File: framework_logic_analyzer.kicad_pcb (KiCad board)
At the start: 4 copper layers, 54 x 43 mm, 116 parts, among them IC1 TXU0104QWBQARQ1, IC2 TXU0104QWBQARQ1, IC3 TXU0104QWBQARQ1, IC4 TXU0104QWBQARQ1, IC5 CYUSB3014-BZXC, IC6 XC9285B18CMR-G, J1 10152803-00011LF, J3 Conn_ARM_JTAG_SWD_10, J4 6101XX249121_610108249121, J5 6101XX249121_610108249121, J6 6101XX249121_610108249121, J7 6101XX249121_610108249121, Q1 MMBT3904, Q2 MMBT3904, Q3 MMBT3904, U1 NCP360SNT1G, U2 TUSB321RWBR, U4 SC189CSKTRT, U5 M24M02-DR, U7 TUSB542RWQR, Y1 19.200 MHz

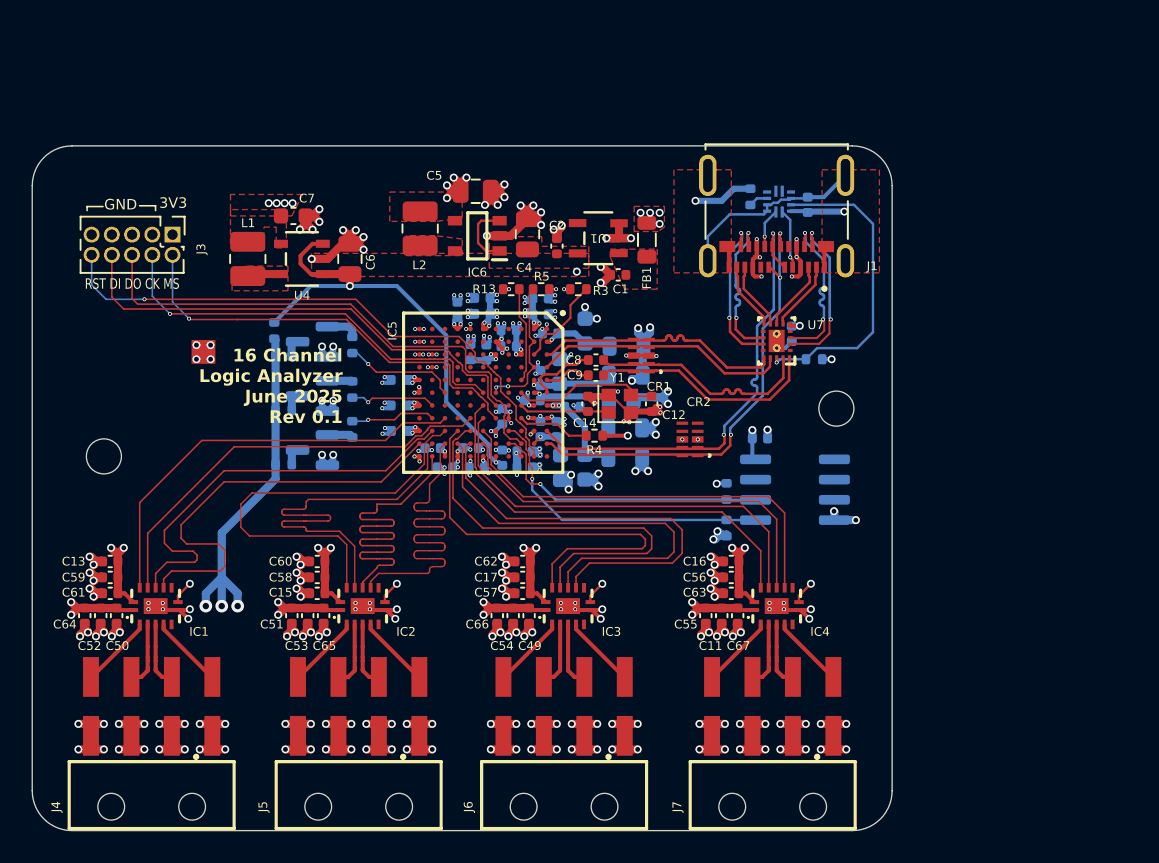
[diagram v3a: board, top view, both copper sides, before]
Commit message: add AC caps for redriver; fix ERC and DRC errors
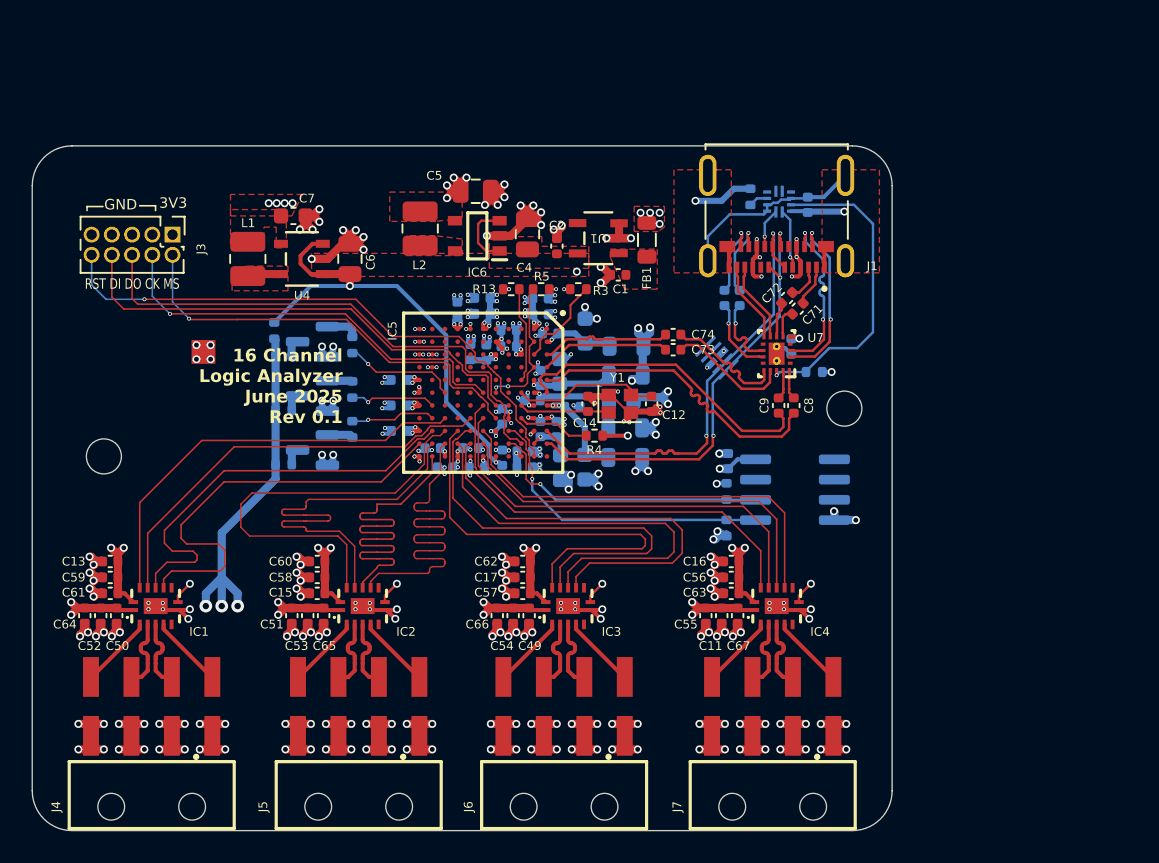
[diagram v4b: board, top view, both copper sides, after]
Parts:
- removed CR1: SP3010-04UTG, SP3010:UDFEN-10_MO229_LTF
- added C69: 100n 25V, Capacitor_SMD:C_0402_1005Metric, B.Cu at (152.9, 72.7)
- added C70: 100n 25V, Capacitor_SMD:C_0402_1005Metric, B.Cu at (153.8, 72.7)
- added C71: 100n 25V, Capacitor_SMD:C_0402_1005Metric, F.Cu at (157.5, 73.3)
- added C72: 100n 25V, Capacitor_SMD:C_0402_1005Metric, F.Cu at (156.8, 72.7)
- added C73: 100n 25V, Capacitor_SMD:C_0402_1005Metric, F.Cu at (149.7, 75.9)
- added C74: 100n 25V, Capacitor_SMD:C_0402_1005Metric, F.Cu at (149.7, 75.0)
- CR2: moved to B.Cu
- moved C8 12.7 mm to (157.2, 79.4), turned to 90 degrees
- moved C9 11.6 mm to (156.3, 79.4), turned to 90 degrees
- moved CR2 5.39 mm to (152.4, 76.4), turned to 45 degrees
- moved C48 2.46 mm to (153.1, 82.9), turned to 90 degrees
- moved C3 0.80 mm to (157.1, 75.7)
- moved U7 0.80 mm to (156.2, 76.2)
- moved R2 0.80 mm to (158.5, 77.3)
- moved H2 0.50 mm to (160.4, 79.6)
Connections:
- C8 pad 1: /USB-C/SS_TX- -> /USB-C/SS_TX+
- C8 pad 2: /SS_AC_TX- -> /USB-C/SS_REDRIVE_TX+
- C9 pad 1: /USB-C/SS_TX+ -> /USB-C/SS_TX-
- C9 pad 2: /SS_AC_TX+ -> /USB-C/SS_REDRIVE_TX-
- IC5 pad A5: /SS_AC_TX+ -> /USB-C/SS_TX+
- IC5 pad A6: /SS_AC_TX- -> /USB-C/SS_TX-
- U7 pad 11: /USB-C/SS_TX2- -> /USB-C/SS_REDRIVE_TX2-
- U7 pad 12: /USB-C/SS_TX2+ -> /USB-C/SS_REDRIVE_TX2+
- U7 pad 14: /USB-C/SS_RX- -> /USB-C/SS_REDRIVE_RX-
- U7 pad 15: /USB-C/SS_RX+ -> /USB-C/SS_REDRIVE_RX+
- U7 pad 17: /USB-C/SS_TX- -> /USB-C/SS_REDRIVE_TX-
- U7 pad 18: /USB-C/SS_TX+ -> /USB-C/SS_REDRIVE_TX+
- U7 pad 6: /USB-C/SS_TX1+ -> /USB-C/SS_REDRIVE_TX1+
- U7 pad 7: /USB-C/SS_TX1- -> /USB-C/SS_REDRIVE_TX1-
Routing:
- net /USB-C/SS_RX+: track 16.0 -> 8.15 mm
- net /USB-C/SS_RX-: track 16.0 -> 8.14 mm
- net /USB-C/SS_REDRIVE_RX+: track 0.00 -> 7.79 mm
- net /USB-C/SS_REDRIVE_RX-: track 0.00 -> 7.75 mm
- net /USB-C/SS_TX-: track 14.4 -> 19.5 mm
- net /USB-C/SS_TX+: track 14.5 -> 19.4 mm
- net /USB-C/SS_TX2+: track 9.88 -> 4.97 mm, vias 2 -> 1
- net /USB-C/SS_REDRIVE_TX2+: track 0.00 -> 4.87 mm, vias 0 -> 1
- net /USB-C/SS_TX2-: track 9.83 -> 4.97 mm, vias 2 -> 1
- net /USB-C/SS_REDRIVE_TX2-: track 0.00 -> 4.84 mm, vias 0 -> 1
- net /SS_AC_TX-: track 4.60 -> 0.00 mm
- net /SS_AC_TX+: track 2.99 -> 0.00 mm
- net /USB-C/SS_REDRIVE_TX1-: track 0.00 -> 2.24 mm
- net /USB-C/SS_TX1-: track 4.46 -> 2.31 mm
- net GND: track 199.1 -> 197.1 mm, vias 267 -> 265
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
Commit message: initial TurboCase implementation
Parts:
- added ?: , Cutout_Pinheader_02x08_254, F.Cu at (129.9, 106.6)
- added ?: , Cutout_Pinheader_02x08_254, F.Cu at (116.9, 106.6)
- added ?: , Cutout_Pinheader_02x08_254, F.Cu at (142.9, 106.6)
- added ?: , Cutout_TypeC, F.Cu at (156.2, 62.6)
- added ?: , Cutout_Pinheader_02x08_254, F.Cu at (155.9, 106.6)

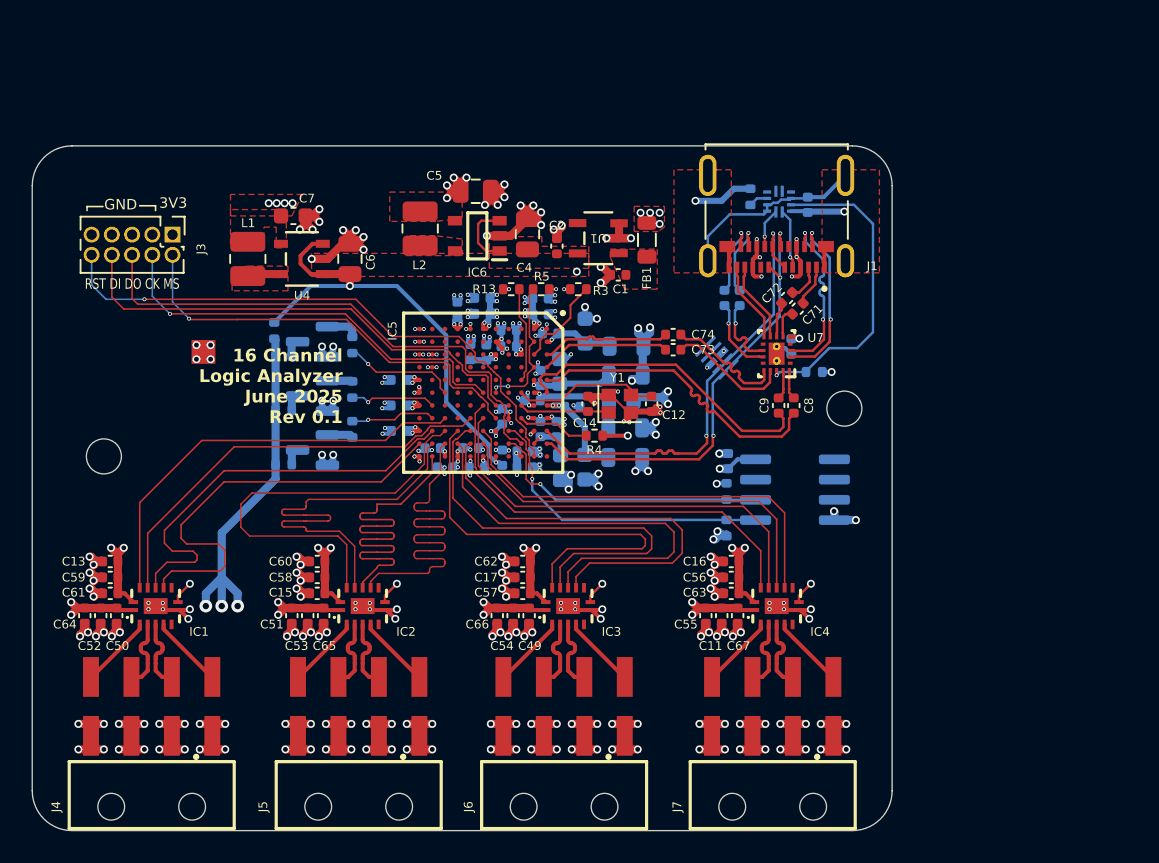
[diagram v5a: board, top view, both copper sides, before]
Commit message: start reworking the usb3c to add ESD and better impedance matching
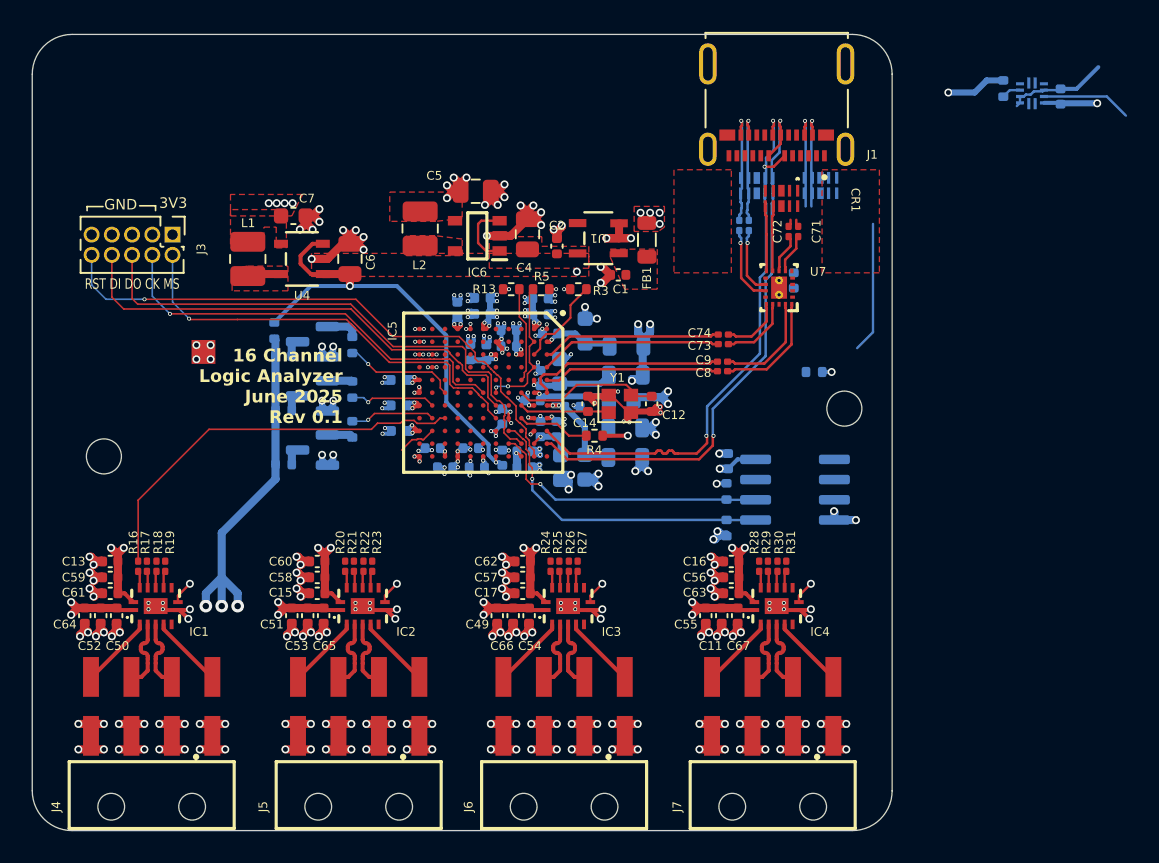
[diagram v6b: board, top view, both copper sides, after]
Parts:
- added CR1: SP3010-04UTG, SP3010:UDFEN-10_MO229_LTF, F.Cu at (156.4, 66.4)
- added CR3: SP3010-04UTG, SP3010:UDFEN-10_MO229_LTF, B.Cu at (158.9, 65.6)
- added R16: 50R 1%, Resistor_SMD:R_0201_0603Metric, F.Cu at (116.0, 89.5)
- added R17: 50R 1%, Resistor_SMD:R_0201_0603Metric, F.Cu at (116.6, 89.5)
- added R18: 50R 1%, Resistor_SMD:R_0201_0603Metric, F.Cu at (117.2, 89.5)
- added R19: 50R 1%, Resistor_SMD:R_0201_0603Metric, F.Cu at (117.8, 89.5)
- added R20: 50R 1%, Resistor_SMD:R_0201_0603Metric, F.Cu at (129.1, 89.5)
- added R21: 50R 1%, Resistor_SMD:R_0201_0603Metric, F.Cu at (129.6, 89.5)
- added R22: 50R 1%, Resistor_SMD:R_0201_0603Metric, F.Cu at (130.2, 89.5)
- added R23: 50R 1%, Resistor_SMD:R_0201_0603Metric, F.Cu at (130.8, 89.5)
- added R24: 50R 1%, Resistor_SMD:R_0201_0603Metric, F.Cu at (141.9, 89.5)
- added R25: 50R 1%, Resistor_SMD:R_0201_0603Metric, F.Cu at (142.5, 89.5)
- added R26: 50R 1%, Resistor_SMD:R_0201_0603Metric, F.Cu at (143.1, 89.5)
- added R27: 50R 1%, Resistor_SMD:R_0201_0603Metric, F.Cu at (143.7, 89.5)
- added R28: 50R 1%, Resistor_SMD:R_0201_0603Metric, F.Cu at (155.1, 89.5)
- added R29: 50R 1%, Resistor_SMD:R_0201_0603Metric, F.Cu at (155.6, 89.5)
- added R30: 50R 1%, Resistor_SMD:R_0201_0603Metric, F.Cu at (156.2, 89.5)
- added R31: 50R 1%, Resistor_SMD:R_0201_0603Metric, F.Cu at (156.8, 89.5)
- C69, C70, C71, C72, C73, C74, C8, C9: footprint Capacitor_SMD:C_0402_1005Metric -> Capacitor_SMD:C_0201_0603Metric
- moved C68 17.3 mm to (174.0, 60.0)
- moved R1 17.3 mm to (170.4, 59.5)
- moved U2 17.3 mm to (172.2, 59.8)
- moved CR2 11.1 mm to (154.9, 65.6), turned to 90 degrees
- moved ? 7.00 mm to (156.2, 55.6)
- moved J1 7.00 mm to (156.2, 58.0)
- moved C8 4.97 mm to (152.8, 77.2), turned to 0 degrees
- moved C71 4.85 mm to (157.5, 68.5), turned to 90 degrees
- moved C69 4.64 mm to (153.8, 68.1)
- moved C70 4.59 mm to (154.4, 68.1)
- moved C9 4.47 mm to (152.8, 76.7), turned to 0 degrees
- moved C72 4.18 mm to (156.9, 68.5), turned to 90 degrees
- moved C3 4.15 mm to (157.2, 71.5)
- moved U7 4.15 mm to (156.3, 72.0)
- moved C73 3.17 mm to (152.8, 75.5)
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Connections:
- CR2 pad 4: unconnected-(CR2-Pad4) -> /USB-C/SS_TX2-
- CR2 pad 5: unconnected-(CR2-Pad5) -> /USB-C/SS_TX2+
- CR2 pad 6: unconnected-(CR2-Pad6) -> /USB-C/SS_TX2+
- CR2 pad 7: unconnected-(CR2-Pad7) -> /USB-C/SS_TX2-
- IC1 pad 10: IN3 -> Net-(IC1-B4Y)
- IC1 pad 11: IN2 -> Net-(IC1-B3Y)
- IC1 pad 12: IN1 -> Net-(IC1-B2Y)
- IC1 pad 13: IN0 -> Net-(IC1-B1Y)
- IC2 pad 10: IN7 -> Net-(IC2-B4Y)
- IC2 pad 11: IN6 -> Net-(IC2-B3Y)
- IC2 pad 12: IN5 -> Net-(IC2-B2Y)
- IC2 pad 13: IN4 -> Net-(IC2-B1Y)
- IC3 pad 10: IN11 -> Net-(IC3-B4Y)
- IC3 pad 11: IN10 -> Net-(IC3-B3Y)
- IC3 pad 12: IN9 -> Net-(IC3-B2Y)
- IC3 pad 13: IN8 -> Net-(IC3-B1Y)
- IC4 pad 10: IN15 -> Net-(IC4-B4Y)
- IC4 pad 11: IN14 -> Net-(IC4-B3Y)
- IC4 pad 12: IN13 -> Net-(IC4-B2Y)
- IC4 pad 13: IN12 -> Net-(IC4-B1Y)
- U5 pad 3: unconnected-(U5-E2-Pad3) -> GND
- U5 pad 7: unconnected-(U5-~{WC}-Pad7) -> GND
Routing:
- net IN11: track 26.7 -> 0.00 mm
- net IN1: track 26.7 -> 0.00 mm
- net IN13: track 26.7 -> 0.00 mm
- net IN12: track 26.7 -> 0.00 mm
- net IN4: track 26.7 -> 0.00 mm
- net IN9: track 26.7 -> 0.00 mm
- net IN3: track 26.7 -> 0.00 mm
- net IN10: track 26.7 -> 0.00 mm
- net IN8: track 26.7 -> 0.00 mm
- net IN15: track 26.7 -> 0.00 mm
- net IN5: track 26.7 -> 0.00 mm
- net IN6: track 26.6 -> 0.00 mm
- net IN7: track 26.6 -> 0.00 mm
- net IN14: track 25.4 -> 0.00 mm
- net IN2: track 26.7 -> 2.46 mm
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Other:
- board size 54 x 43 mm -> 54 x 50 mm

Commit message: start implementing SML feedback
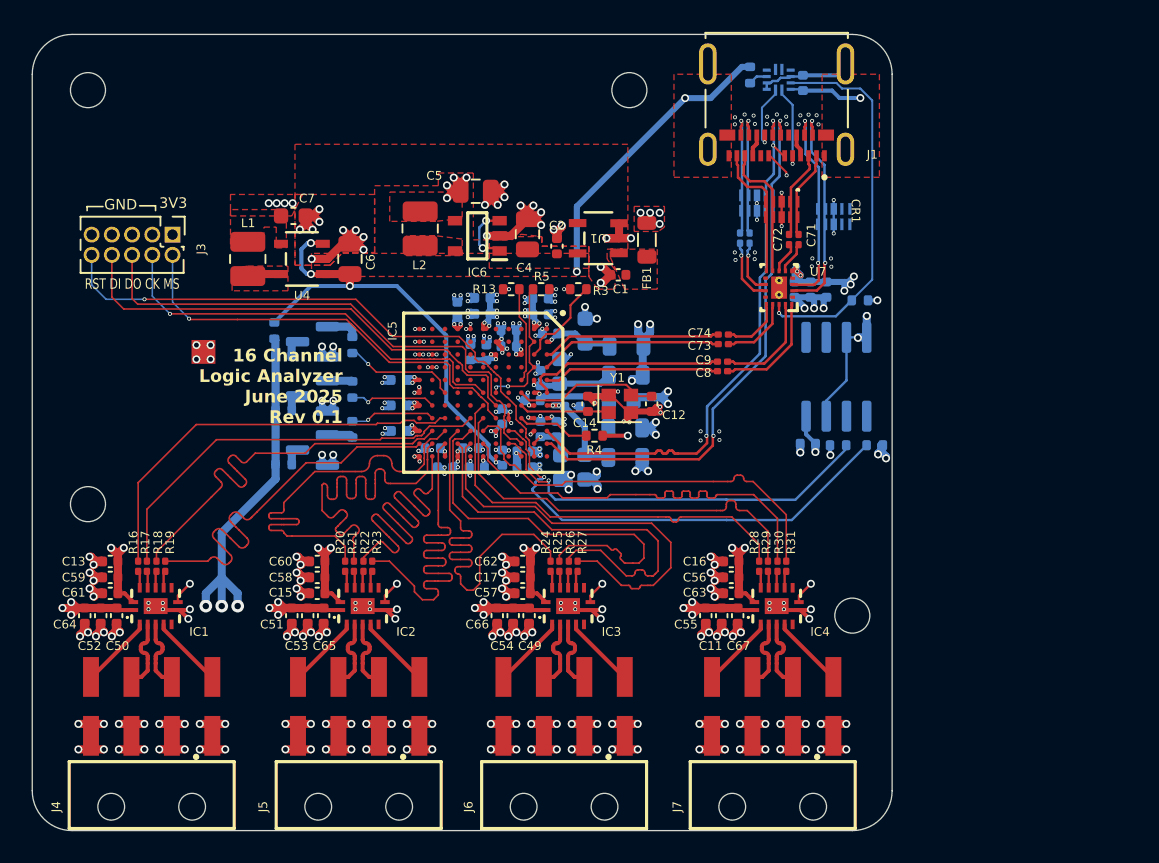
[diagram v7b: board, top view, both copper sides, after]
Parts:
- added C75: 100nF, Capacitor_SMD:C_0402_1005Metric, B.Cu at (157.3, 72.1)
- added C76: 1u, Capacitor_SMD:C_0402_1005Metric, B.Cu at (159.3, 72.1)
- added H3: MountingHole, MountingHole:MountingHole_2.2mm_M2, F.Cu at (112.9, 59.6)
- added H4: MountingHole, MountingHole:MountingHole_2.2mm_M2, F.Cu at (146.9, 59.6)
- moved C68 16.2 mm to (157.8, 59.1)
- moved U2 15.9 mm to (156.3, 58.9)
- moved R1 15.9 mm to (154.5, 58.6)
- moved H2 13.0 mm to (160.9, 92.6)
- moved R14 10.7 mm to (162.3, 81.9), turned to 180 degrees
- moved R15 7.58 mm to (160.0, 81.9), turned to 0 degrees
- moved U5 7.55 mm to (159.9, 77.6), turned to -90 degrees
- moved R2 5.34 mm to (161.4, 72.8)
- moved C48 5.13 mm to (158.1, 81.8), turned to 180 degrees
- moved H1 3.16 mm to (112.9, 85.6)
- moved CR3 2.12 mm to (159.7, 67.5)
- moved C49 2.00 mm to (140.6, 92.6)
- moved C3 1.20 mm to (158.3, 72.1)
- moved CR2 1.09 mm to (154.9, 66.7)
- moved C17 1.00 mm to (140.2, 90.2)
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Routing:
- net IN1: track 0.00 -> 26.0 mm
- net IN11: track 0.00 -> 26.0 mm
- net IN9: track 0.00 -> 26.0 mm
- net IN12: track 0.00 -> 26.0 mm
- net IN10: track 0.00 -> 26.0 mm
- net IN15: track 0.00 -> 26.0 mm
- net IN13: track 0.00 -> 26.0 mm
- net IN14: track 0.00 -> 25.9 mm
- net IN8: track 0.00 -> 25.9 mm
- net IN3: track 0.00 -> 25.9 mm
- net IN4: track 0.00 -> 25.9 mm
- net IN7: track 0.00 -> 25.9 mm
- net IN6: track 0.00 -> 25.9 mm
- net IN5: track 0.00 -> 25.8 mm
- net IN2: track 2.46 -> 25.9 mm
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- added copper zone on In2.Cu, net GND
- removed copper zone on In2.Cu, net /USB-C/VBUS_CON_IN
